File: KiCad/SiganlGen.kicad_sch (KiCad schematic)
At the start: 9 parts, among them J1 Barrel_Jack_MountingPin, J8 Screw_Terminal_01x03, U1 RaspberryPi_Pico

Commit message: Changed footprints, arrangement of elements on pcb
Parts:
- D10, D9: footprint Diode_SMD:D_SOD-523 -> Diode_THT:D_DO-41_SOD81_P10.16mm_Horizontal
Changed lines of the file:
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@@
 			)
 		)
-		(property "Footprint" "Diode_SMD:D_SOD-523"
+		(property "Footprint" "Diode_THT:D_DO-41_SOD81_P10.16mm_Horizontal"
 			(at 41.275 59.69 0)
 			(effects
@@
 			)
 		)
-		(property "Footprint" "Diode_SMD:D_SOD-523"
+		(property "Footprint" "Diode_THT:D_DO-41_SOD81_P10.16mm_Horizontal"
 			(at 23.495 86.36 0)
 			(effects

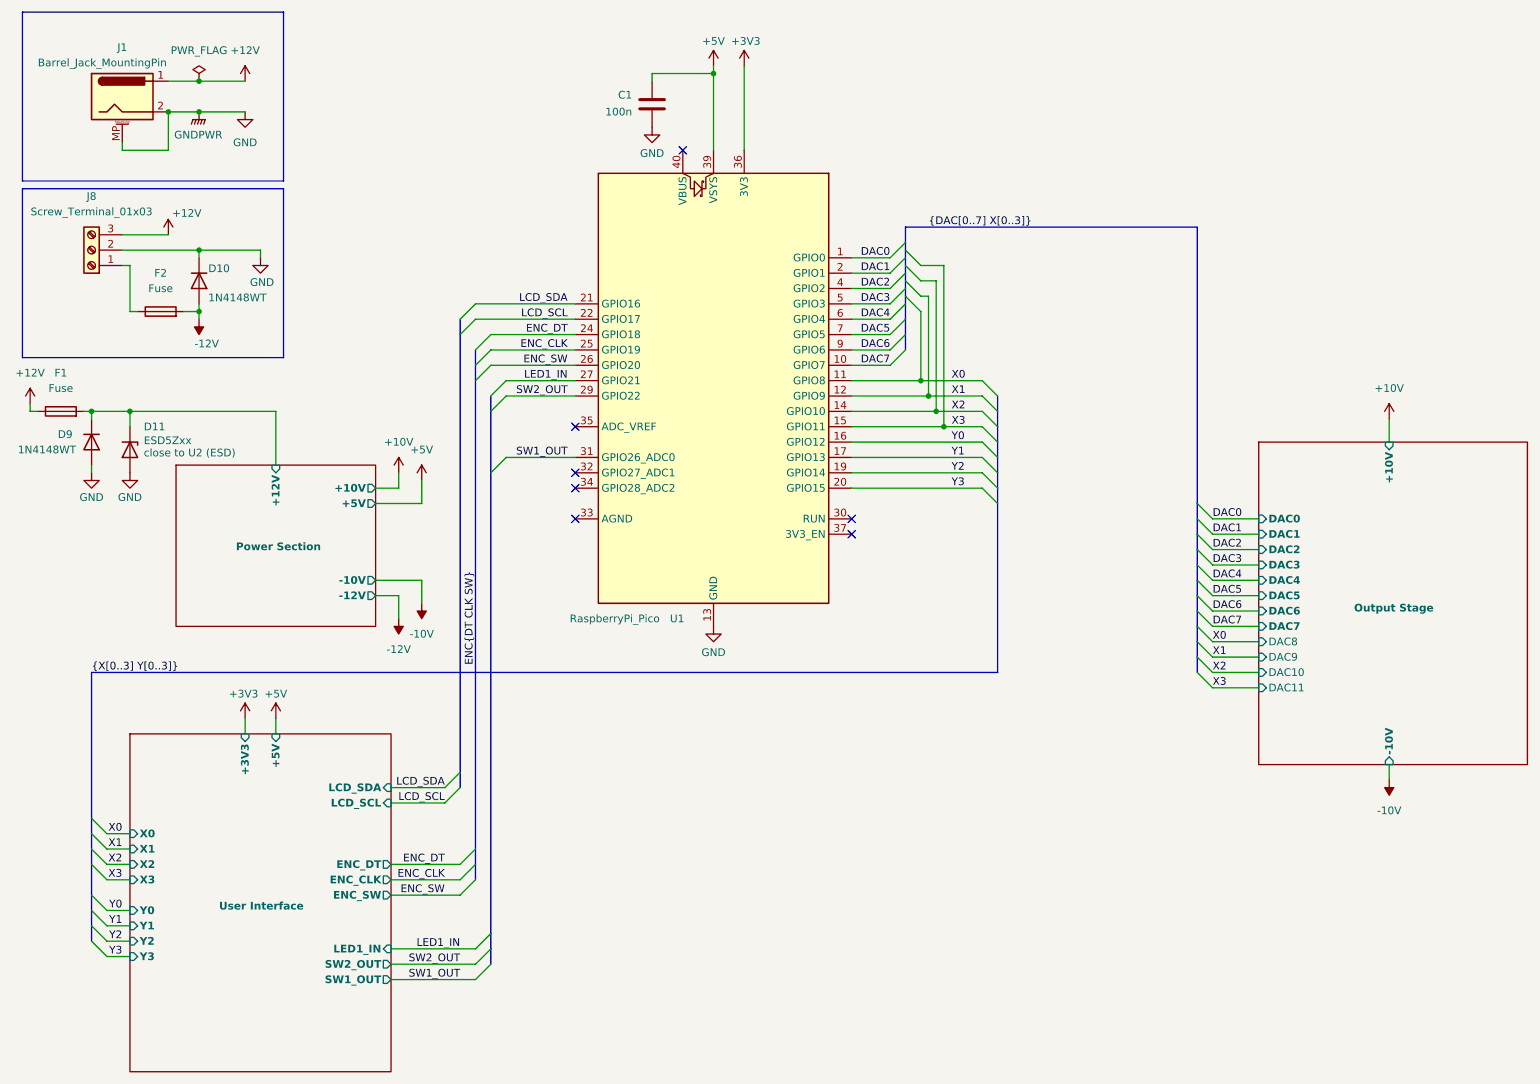
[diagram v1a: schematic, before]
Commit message: Tidied up schematic, changed footprints
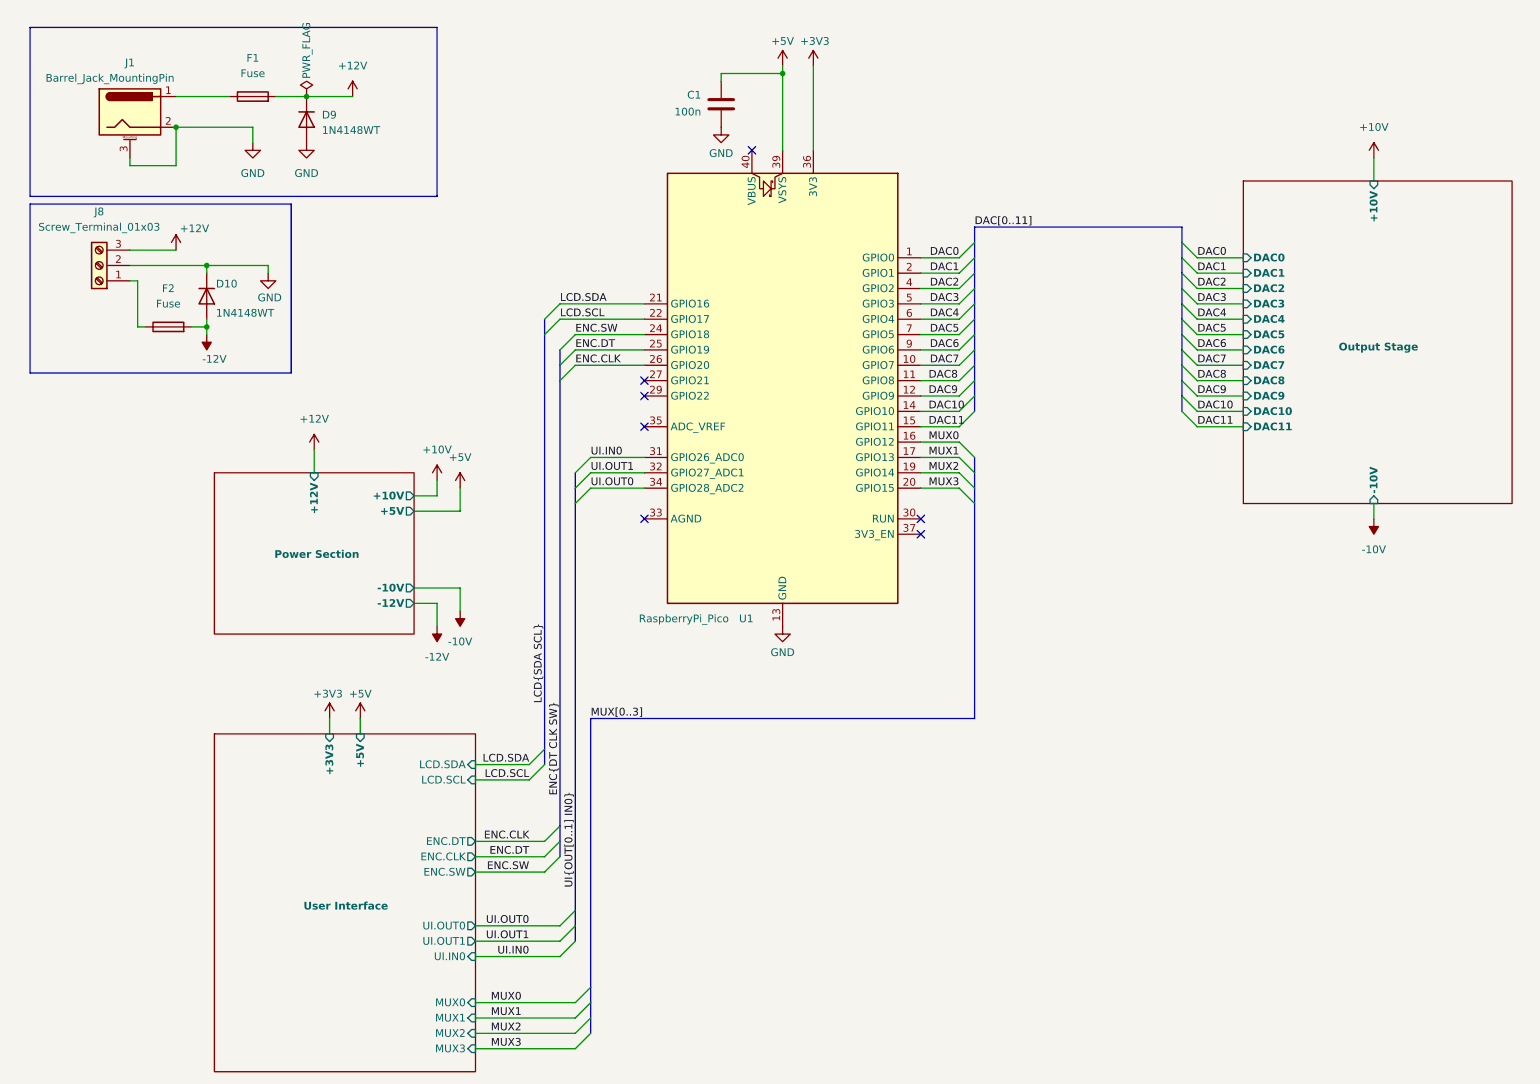
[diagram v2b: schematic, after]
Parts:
- removed D11: ESD5Zxx, Diode_SMD:D_SOD-523, symbol Diode:ESD5Zxx
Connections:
- net Power Section/+12V is gone; now on net +12V: D9.1 (K), F1.2
- net +12V: no longer F1.1, J1.1
- net GND: now also J1.3 (MountPin); no longer J1.MP (MountPin)
- net UI.OUT1: now reaches U1.32 (GPIO27_ADC1)
- net UI.OUT0: now reaches U1.34 (GPIO28_ADC2)
- net ENC_CLK renamed ENC.DT
- net ENC_DT renamed ENC.SW
- net ENC_SW renamed ENC.CLK
- net LCD_SCL renamed LCD.SCL
- net LCD_SDA renamed LCD.SDA
- net LED1_IN: no longer names the net of U1.27 (GPIO21)
- net SW1_OUT renamed UI.IN0
- net SW2_OUT: no longer names the net of U1.29 (GPIO22)
- net X0 renamed DAC8
- net X1 renamed DAC9
- net X2 renamed DAC10
- net X3 renamed DAC11
- net Y0 renamed MUX0
- net Y1 renamed MUX1
- net Y2 renamed MUX2
- net Y3 renamed MUX3
- new net: F1.1, J1.1
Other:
- sheet User Interface ports: added ENC.CLK, ENC.DT, ENC.SW, LCD.SCL, LCD.SDA, MUX0, MUX1, MUX2, MUX3, UI.IN0, UI.OUT0, UI.OUT1; removed ENC_CLK, ENC_DT, ENC_SW, LCD_SCL, LCD_SDA, LED1_IN, SW1_OUT, SW2_OUT, X0, X1, X2, X3, Y0, Y1, Y2, Y3
- moved on the sheet: C1, D10, F2, J1, J8, U1

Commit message: PCB design
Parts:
- removed D10: 1N4148WT, Diode_THT:D_DO-41_SOD81_P10.16mm_Horizontal, symbol Diode:1N4148WT
- removed F2: Fuse, Fuse:Fuseholder_Clip-5x20mm_Keystone_3517_Inline_P23.11x6.76mm_D1.70mm_Horizontal, symbol Device:Fuse
- removed J8: Screw_Terminal_01x03, TerminalBlock_MetzConnect:TerminalBlock_MetzConnect_Type094_RT03503HBLU_1x03_P5.00mm_Horizontal, symbol Connector:Screw_Terminal_01x03
- D1: renamed from D9; footprint Diode_THT:D_DO-41_SOD81_P10.16mm_Horizontal -> Diode_THT:D_DO-41_SOD81_P5.08mm_Vertical_KathodeUp
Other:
- moved on the sheet: D1, F1, J1

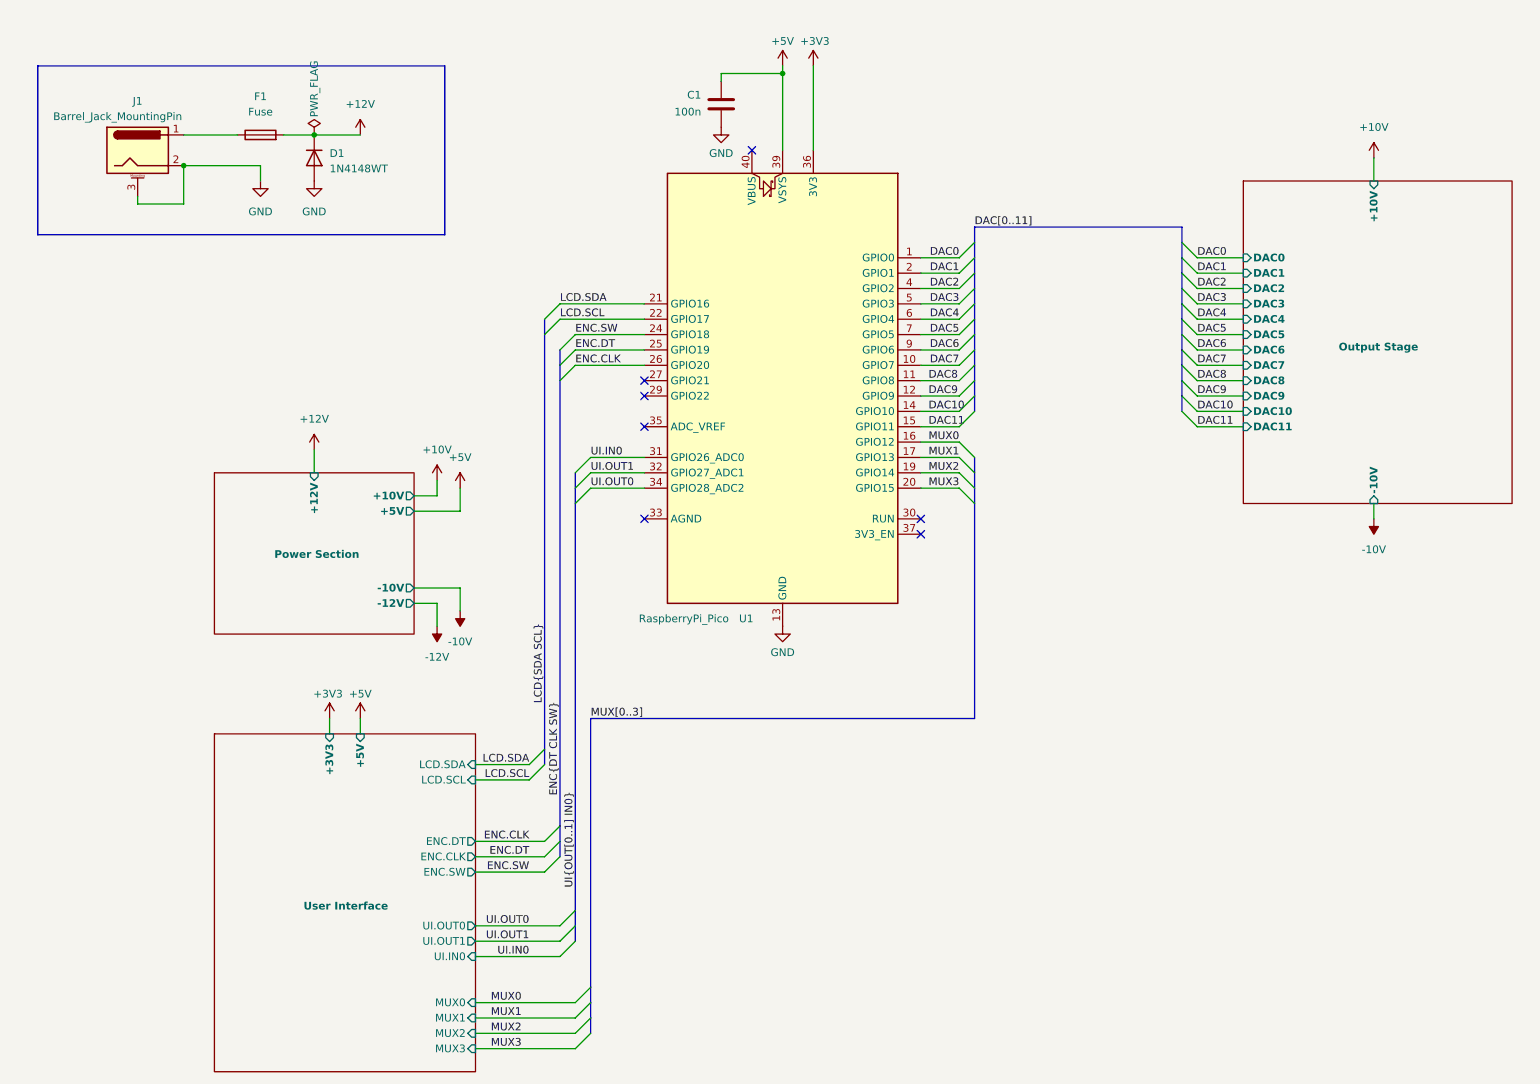
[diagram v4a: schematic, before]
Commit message: output sim, filter sim, filter sch, output change
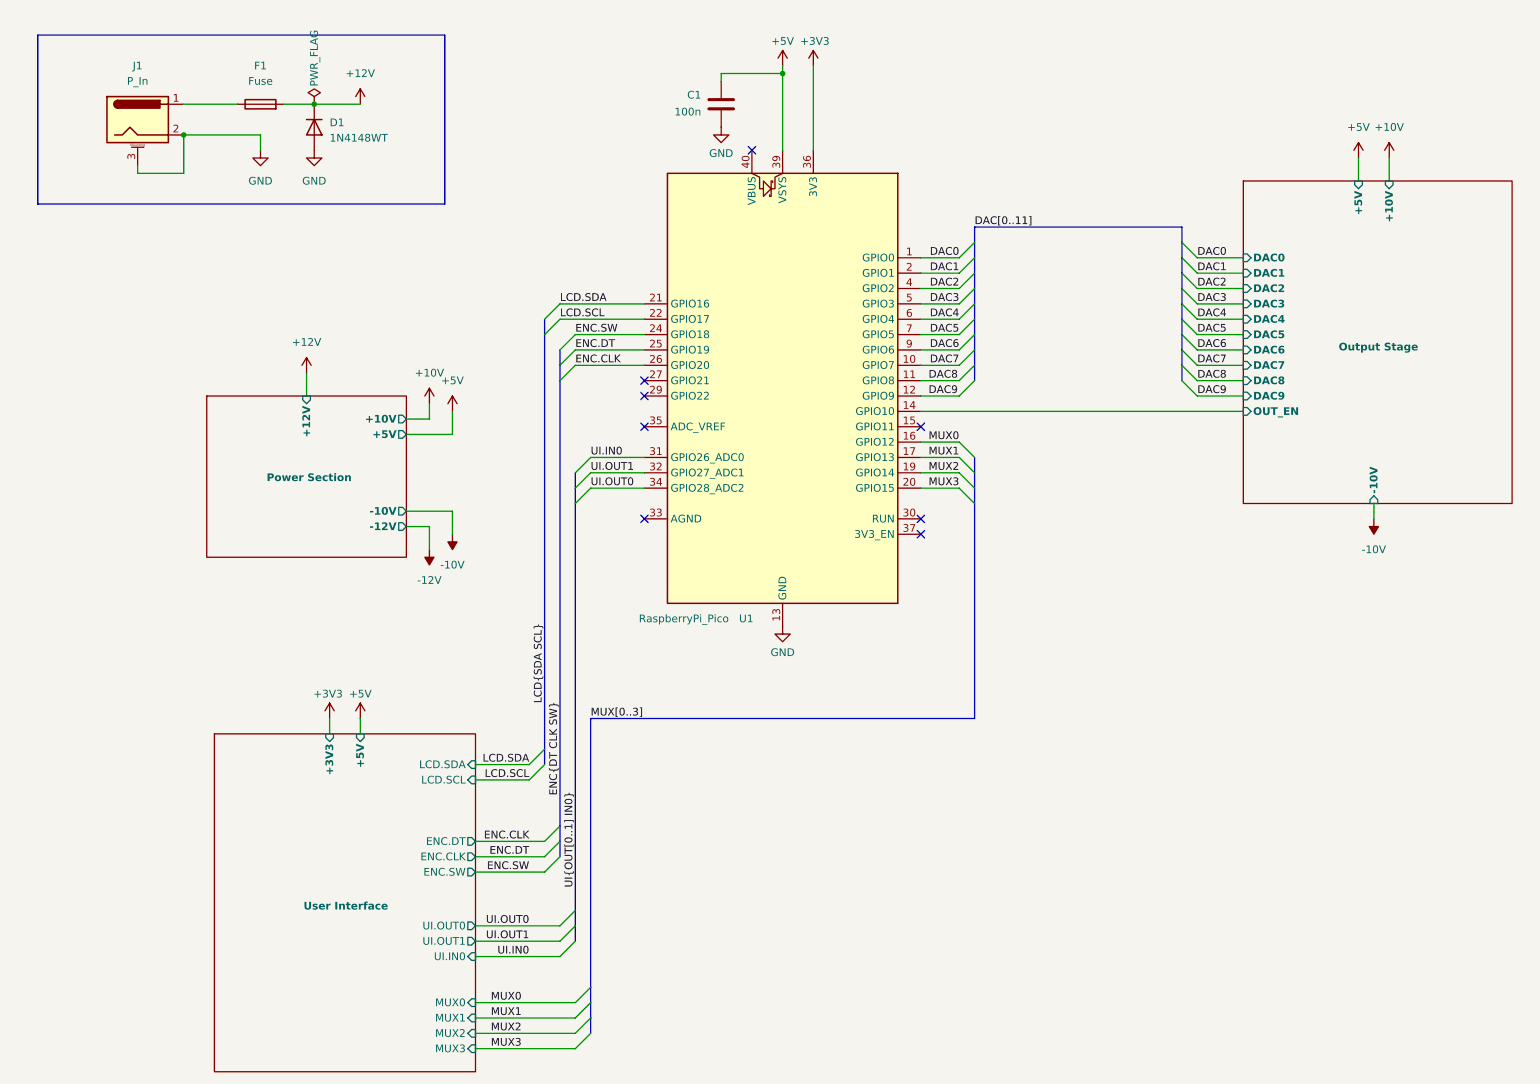
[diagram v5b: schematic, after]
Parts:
- J1: value Barrel_Jack_MountingPin -> P_In
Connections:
- net DAC10 renamed Output Stage/OUT_EN
- net DAC11: no longer names the net of U1.15 (GPIO11)
- no-connect marks 7 -> 8
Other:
- sheet Output Stage ports: added +5V, OUT_EN; removed DAC10, DAC11
- moved on the sheet: D1, F1, J1

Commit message: Final PCB version (probably)
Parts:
- removed D1: 1N4148WT, Diode_THT:D_DO-41_SOD81_P5.08mm_Vertical_KathodeUp, symbol Diode:1N4148WT
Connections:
- net Output Stage/OUT_EN: now also U1.15 (GPIO11); no longer U1.14 (GPIO10)
- new net Output Stage/3.3Sig: U1.14 (GPIO10)
- no-connect marks 8 -> 7
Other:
- sheet Output Stage ports: added 3.3Sig; removed none
- moved on the sheet: F1
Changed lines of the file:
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@@
 	)
 	(junction
-		(at 64.77 30.48)
+		(at 59.69 30.48)
 		(diameter 0)
 		(color 0 0 0 0)
@@
 	)
 	(no_connect
-		(at 165.1 83.82)
-	)
-	(no_connect
 		(at 119.38 83.82)
 	)
@@
 		)
 	)
+	(wire
+		(pts
+			(xy 165.1 81.28) (xy 218.44 81.28)
+		)
+		(stroke
+			(width 0)
+			(type default)
+		)
+	)
 	(bus
 		(pts
@@
 	(wire
 		(pts
-			(xy 43.18 30.48) (xy 52.07 30.48)
+			(xy 43.18 30.48) (xy 46.99 30.48)
 		)
 		(stroke
@@
 	(wire
 		(pts
-			(xy 64.77 30.48) (xy 72.39 30.48)
+			(xy 59.69 30.48) (xy 67.31 30.48)
 		)
 		(stroke
@@
 	(wire
 		(pts
-			(xy 165.1 81.28) (xy 218.44 81.28)
-		)
-		(stroke
-			(width 0)
-			(type default)
-		)
-	)
-	(wire
-		(pts
 			(xy 80.01 82.55) (xy 83.82 82.55)
 		)
@@
 	(wire
 		(pts
+			(xy 165.1 83.82) (xy 218.44 83.82)
+		)
+		(stroke
+			(width 0)
+			(type default)
+		)
+	)
+	(wire
+		(pts
 			(xy 210.82 76.2) (xy 218.44 76.2)
 		)
@@
 	(wire
 		(pts
-			(xy 59.69 30.48) (xy 64.77 30.48)
+			(xy 54.61 30.48) (xy 59.69 30.48)
 		)
 		(stroke
@@
 	(symbol
 		(lib_id "power:+12V")
-		(at 72.39 30.48 0)
+		(at 67.31 30.48 0)
 		(unit 1)
 		(exclude_from_sim no)
@@
 		(fields_autoplaced yes)
 		(property "Reference" "#PWR05"
-			(at 72.39 34.29 0)
+			(at 67.31 34.29 0)
 			(effects
 				(font
@@
 		)
 		(property "Value" "+12V"
-			(at 72.39 25.4 0)
+			(at 67.31 25.4 0)
 			(effects
 				(font
@@
 		)
 		(property "Footprint" ""
-			(at 72.39 30.48 0)
+			(at 67.31 30.48 0)
 			(effects
 				(font
@@
 		)
 		(property "Datasheet" ""
-			(at 72.39 30.48 0)
+			(at 67.31 30.48 0)
 			(effects
 				(font
@@
 		)
 		(property "Description" "Power symbol creates a global label with name \"+12V\""
-			(at 72.39 30.48 0)
+			(at 67.31 30.48 0)
 			(effects
 				(font
@@
 	)
 	(symbol
-		(lib_id "Diode:1N4148WT")
-		(at 64.77 34.29 270)
-		(unit 1)
-		(exclude_from_sim no)
-		(in_bom yes)
-		(on_board yes)
-		(dnp no)
-		(property "Reference" "D1"
-			(at 67.31 33.528 90)
-			(effects
-				(font
-					(size 1.27 1.27)
-				)
-				(justify left)
-			)
-		)
-		(property "Value" "1N4148WT"
-			(at 67.31 36.068 90)
-			(effects
-				(font
-					(size 1.27 1.27)
-				)
-				(justify left)
-			)
-		)
-		(property "Footprint" "Diode_THT:D_DO-41_SOD81_P5.08mm_Vertical_KathodeUp"
-			(at 60.325 34.29 0)
-			(effects
-				(font
-					(size 1.27 1.27)
-				)
-				(hide yes)
-			)
-		)
-		(property "Datasheet" "https://www.diodes.com/assets/Datasheets/ds30396.pdf"
-			(at 64.77 34.29 0)
-			(effects
-				(font
-					(size 1.27 1.27)
-				)
-				(hide yes)
-			)
-		)
-		(property "Description" "75V 0.15A Fast switching Diode, SOD-523"
-			(at 64.77 34.29 0)
-			(effects
-				(font
-					(size 1.27 1.27)
-				)
-				(hide yes)
-			)
-		)
-		(property "Sim.Device" "D"
-			(at 64.77 34.29 0)
-			(effects
-				(font
-					(size 1.27 1.27)
-				)
-				(hide yes)
-			)
-		)
-		(property "Sim.Pins" "1=K 2=A"
-			(at 64.77 34.29 0)
-			(effects
-				(font
-					(size 1.27 1.27)
-				)
-				(hide yes)
-			)
-		)
-		(pin "2"
-		)
-		(pin "1"
-		)
-		(instances
-			(project "SiganlGen"
-				(path "/e2db369b-fed9-4358-b449-15db5155edf2"
-					(reference "D1")
-					(unit 1)
-				)
-			)
-		)
-	)
-	(symbol
 		(lib_id "power:-10V")
 		(at 87.63 101.6 180)
@@
 	(symbol
 		(lib_id "power:PWR_FLAG")
-		(at 64.77 30.48 0)
+		(at 59.69 30.48 0)
 		(unit 1)
 		(exclude_from_sim no)
@@
 		(dnp no)
 		(property "Reference" "#FLG01"
-			(at 64.77 28.575 0)
+			(at 59.69 28.575 0)
 			(effects
 				(font
@@
 		)
 		(property "Value" "PWR_FLAG"
-			(at 64.77 22.86 90)
+			(at 59.69 22.86 90)
 			(effects
 				(font
@@
 		)
 		(property "Footprint" ""
-			(at 64.77 30.48 0)
+			(at 59.69 30.48 0)
 			(effects
 				(font
@@
 		)
 		(property "Datasheet" "~"
-			(at 64.77 30.48 0)
+			(at 59.69 30.48 0)
 			(effects
 				(font
@@
 		)
 		(property "Description" "Special symbol for telling ERC where power comes from"
-			(at 64.77 30.48 0)
+			(at 59.69 30.48 0)
 			(effects
 				(font
@@
 	)
 	(symbol
-		(lib_id "power:GND")
-		(at 64.77 38.1 0)
-		(unit 1)
-		(exclude_from_sim no)
-		(in_bom yes)
-		(on_board yes)
-		(dnp no)
-		(fields_autoplaced yes)
-		(property "Reference" "#PWR03"
-			(at 64.77 44.45 0)
-			(effects
-				(font
-					(size 1.27 1.27)
-				)
-				(hide yes)
-			)
-		)
-		(property "Value" "GND"
-			(at 64.77 43.18 0)
-			(effects
-				(font
-					(size 1.27 1.27)
-				)
-			)
-		)
-		(property "Footprint" ""
-			(at 64.77 38.1 0)
-			(effects
-				(font
-					(size 1.27 1.27)
-				)
-				(hide yes)
-			)
-		)
-		(property "Datasheet" ""
-			(at 64.77 38.1 0)
-			(effects
-				(font
-					(size 1.27 1.27)
-				)
-				(hide yes)
-			)
-		)
-		(property "Description" "Power symbol creates a global label with name \"GND\" , ground"
-			(at 64.77 38.1 0)
-			(effects
-				(font
-					(size 1.27 1.27)
-				)
-				(hide yes)
-			)
-		)
-		(pin "1"
-		)
-		(instances
-			(project "SiganlGen"
-				(path "/e2db369b-fed9-4358-b449-15db5155edf2"
-					(reference "#PWR03")
-					(unit 1)
-				)
-			)
-		)
-	)
-	(symbol
 		(lib_id "power:+10V")
 		(at 242.57 39.37 0)
@@
 	(symbol
 		(lib_id "Device:Fuse")
-		(at 55.88 30.48 90)
+		(at 50.8 30.48 90)
 		(unit 1)
 		(exclude_from_sim no)
@@
 		(fields_autoplaced yes)
 		(property "Reference" "F1"
-			(at 55.88 24.13 90)
+			(at 50.8 24.13 90)
 			(effects
 				(font
@@
 		)
 		(property "Value" "Fuse"
-			(at 55.88 26.67 90)
+			(at 50.8 26.67 90)
 			(effects
 				(font
@@
 		)
 		(property "Footprint" "Fuse:Fuseholder_Clip-5x20mm_Keystone_3517_Inline_P23.11x6.76mm_D1.70mm_Horizontal"
-			(at 55.88 32.258 90)
+			(at 50.8 32.258 90)
 			(effects
 				(font
@@
 		)
 		(property "Datasheet" "~"
-			(at 55.88 30.48 0)
+			(at 50.8 30.48 0)
 			(effects
 				(font
@@
 		)
 		(property "Description" "Fuse"
-			(at 55.88 30.48 0)
+			(at 50.8 30.48 0)
 			(effects
 				(font
@@
 		)
 		(pin "OUT_EN" input
+			(at 218.44 83.82 180)
+			(effects
+				(font
+					(size 1.27 1.27)
+					(bold yes)
+				)
+				(justify left)
+			)
+		)
+		(pin "3.3Sig" input
 			(at 218.44 81.28 180)
 			(effects
